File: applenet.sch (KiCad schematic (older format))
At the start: 112 parts, among them J1 6PIN, P1 LISA_BUS, T1 157-0019, T2 157-0020, Y1 Crystal

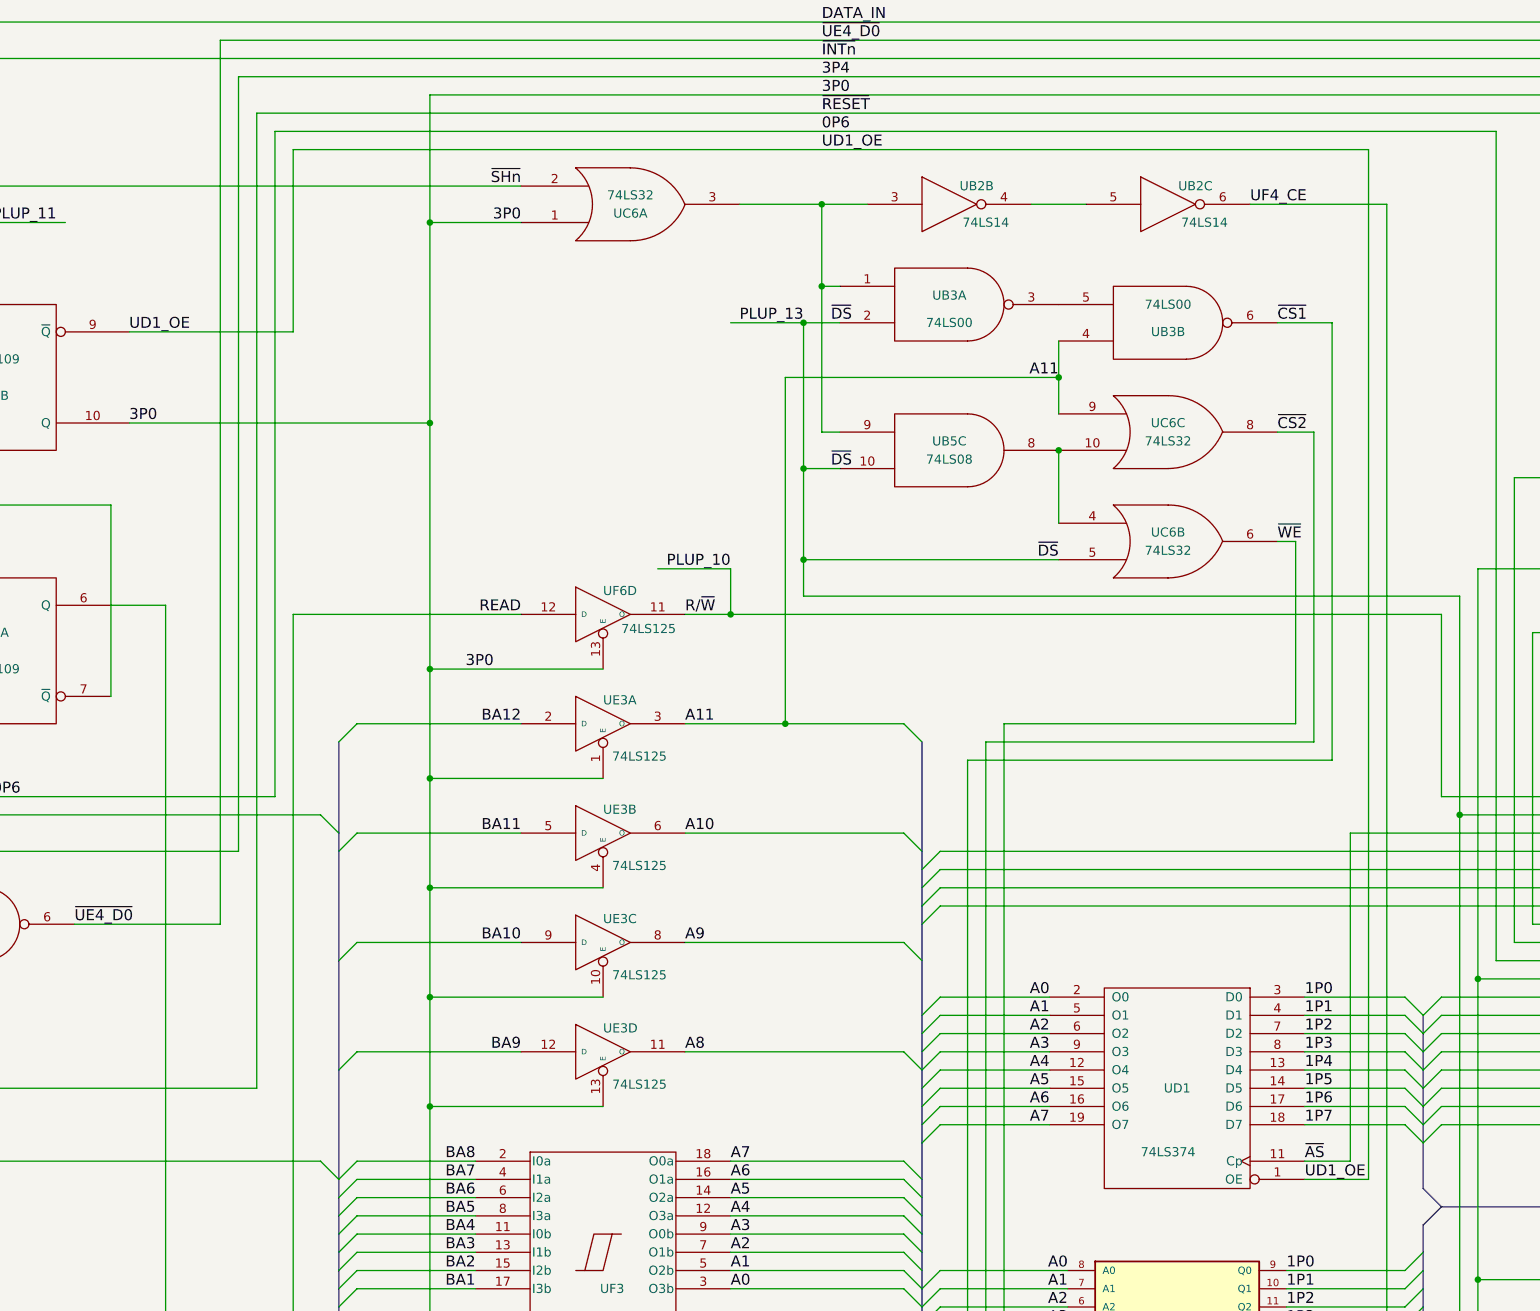
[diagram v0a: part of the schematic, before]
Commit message: Correct input to UC6B.
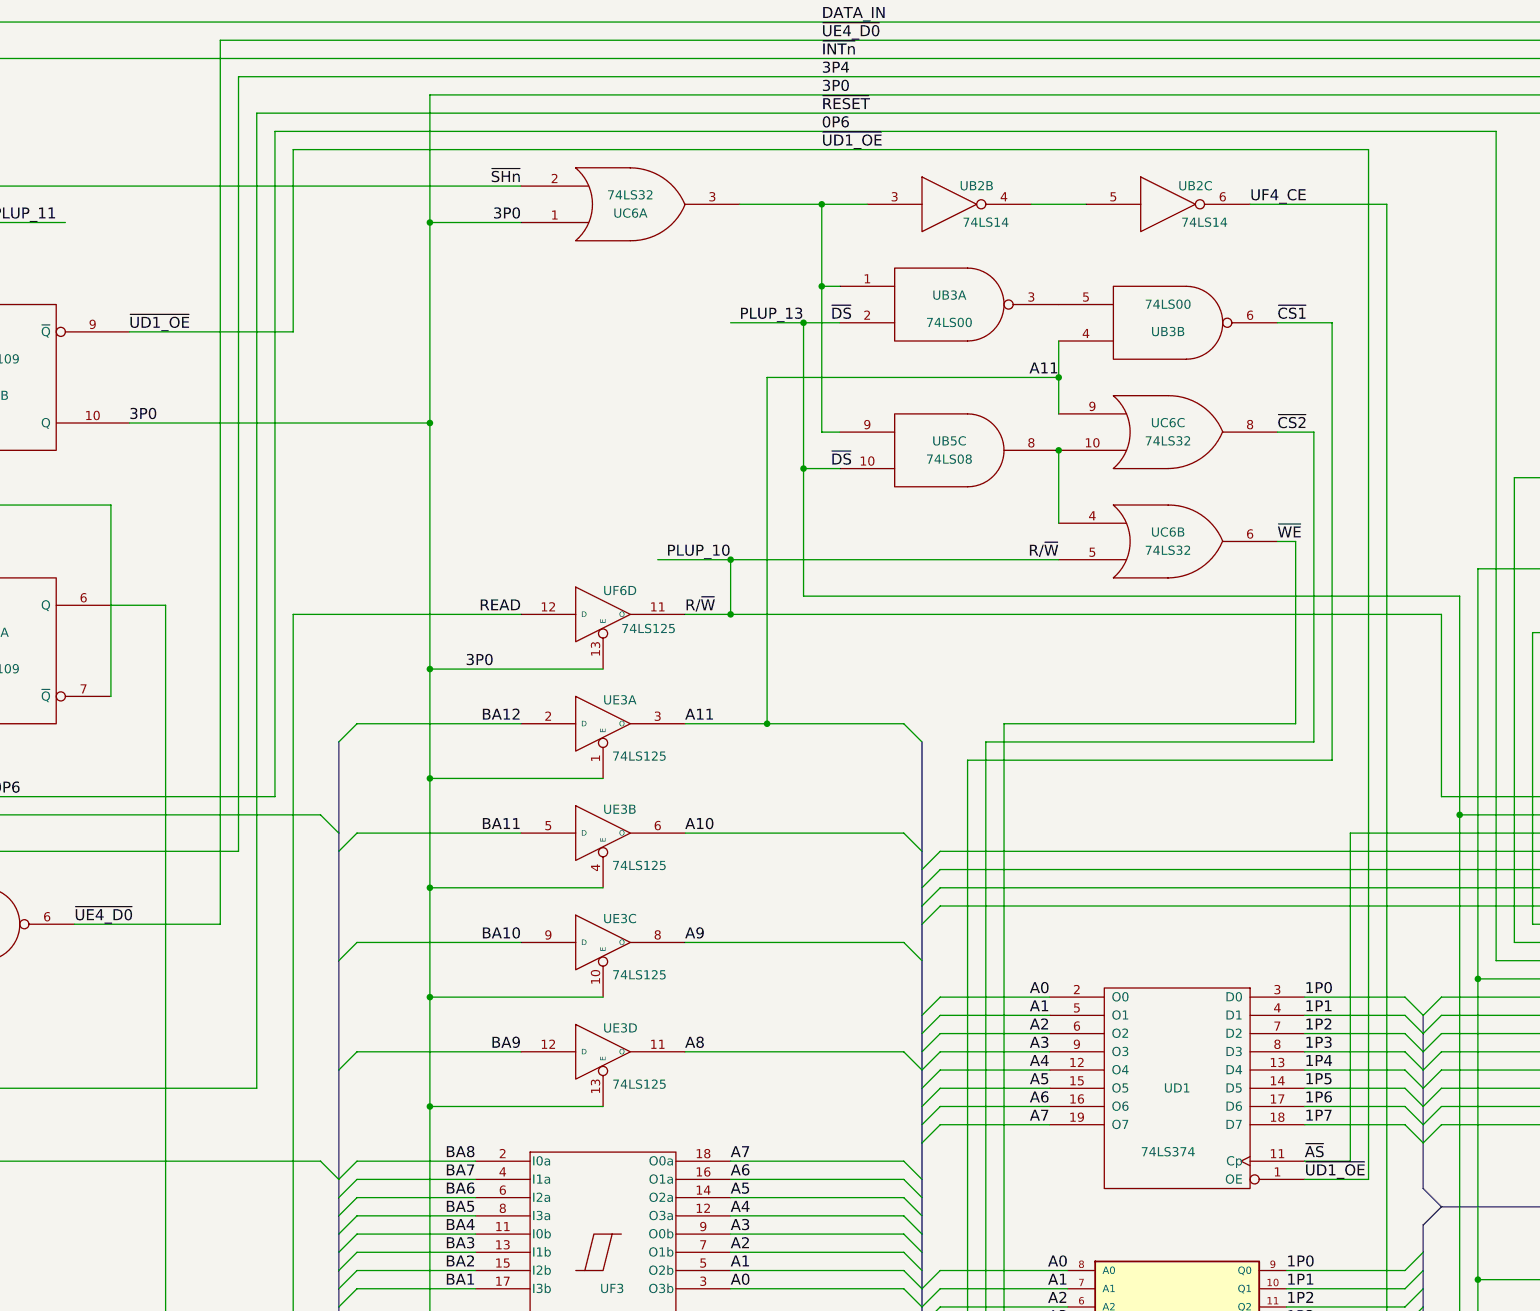
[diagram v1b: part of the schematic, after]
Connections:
- net PLUP_10: now also UC6.5
- net PLUP_13: no longer UC6.5
- net UD1_OE renamed ~UD1_OE
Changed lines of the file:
@@
 Title "Inferred schematic for the AppleNet network adaptor for Lisa"
 Date "2018-11-25"
-Rev "000 (DRAFT!)"
+Rev "001 (DRAFT!)"
 Comp ""
 Comment1 "London"
@@
 ~AS
 Text Label 12500 7550 0    60   ~ 0
-UD1_OE
+~UD1_OE
 Text Label 6050 2900 0    60   ~ 0
-UD1_OE
+~UD1_OE
 Text Label 6050 3400 0    60   ~ 0
 3P0
@@
 ~DS
 Text Label 11150 4150 2    60   ~ 0
-~DS
+R/~W
 Text Label 18450 4900 2    60   ~ 0
 DATA_OUT
@@
 Text Label 18450 5300 0    60   ~ 0
 PLUP_15
-Text Label 9350 4200 2    60   ~ 0
+Text Label 9350 4150 2    60   ~ 0
 PLUP_10
 Text Label 15100 2600 2    60   ~ 0
@@
 ~RESET
 Text Label 9850 1900 0    60   ~ 0
-UD1_OE
+~UD1_OE
 Text Label 9850 1800 0    60   ~ 0
 0P6
@@
 Wire Wire Line
 	9750 4350 13350 4350
+Connection ~ 9550 5050
 Wire Wire Line
-	9750 4150 11150 4150
-Connection ~ 9650 5050
-Wire Wire Line
-	9650 3150 9650 5050
+	9550 3150 9550 5050
 Wire Wire Line
 	12750 7450 12750 5650
@@
 Connection ~ 16800 16600
 Wire Wire Line
-	9100 5050 9650 5050
+	9100 5050 9550 5050
 Wire Wire Line
-	9650 5050 10300 5050
+	9550 5050 10300 5050
 Wire Wire Line
 	7300 6850 8200 6850
@@
 	2250 7450 4100 7450
 Wire Wire Line
-	9650 3150 11150 3150
+	9550 3150 11150 3150
 Wire Wire Line
 	10500 6050 14150 6050
@@
 	9750 2850 9750 3650
 Wire Wire Line
-	9750 3650 9750 4150
+	9750 3650 9750 4350
 Wire Wire Line
-	9750 4150 9750 4350
-Wire Wire Line
-	9950 3650 9750 3650
+	9750 3650 9950 3650
 Wire Wire Line
 	9850 3450 9950 3450
@@
 	8200 2300 7700 2300
 Connection ~ 9750 2850
-Connection ~ 9750 4150
 Connection ~ 18400 5300
 Wire Wire Line
-	9350 4450 9350 4200
+	9350 4450 9350 4150
 Connection ~ 9350 4450
 Wire Wire Line
-	9350 4200 8950 4200
+	8950 4150 9350 4150
+Wire Wire Line
+	9350 4150 11150 4150
 Wire Wire Line
 	1900 4000 2250 4000
@@
 Text Notes 8400 17600 0    138  ~ 0
 CHUNNEL
+Connection ~ 9350 4150
 $EndSCHEMATC

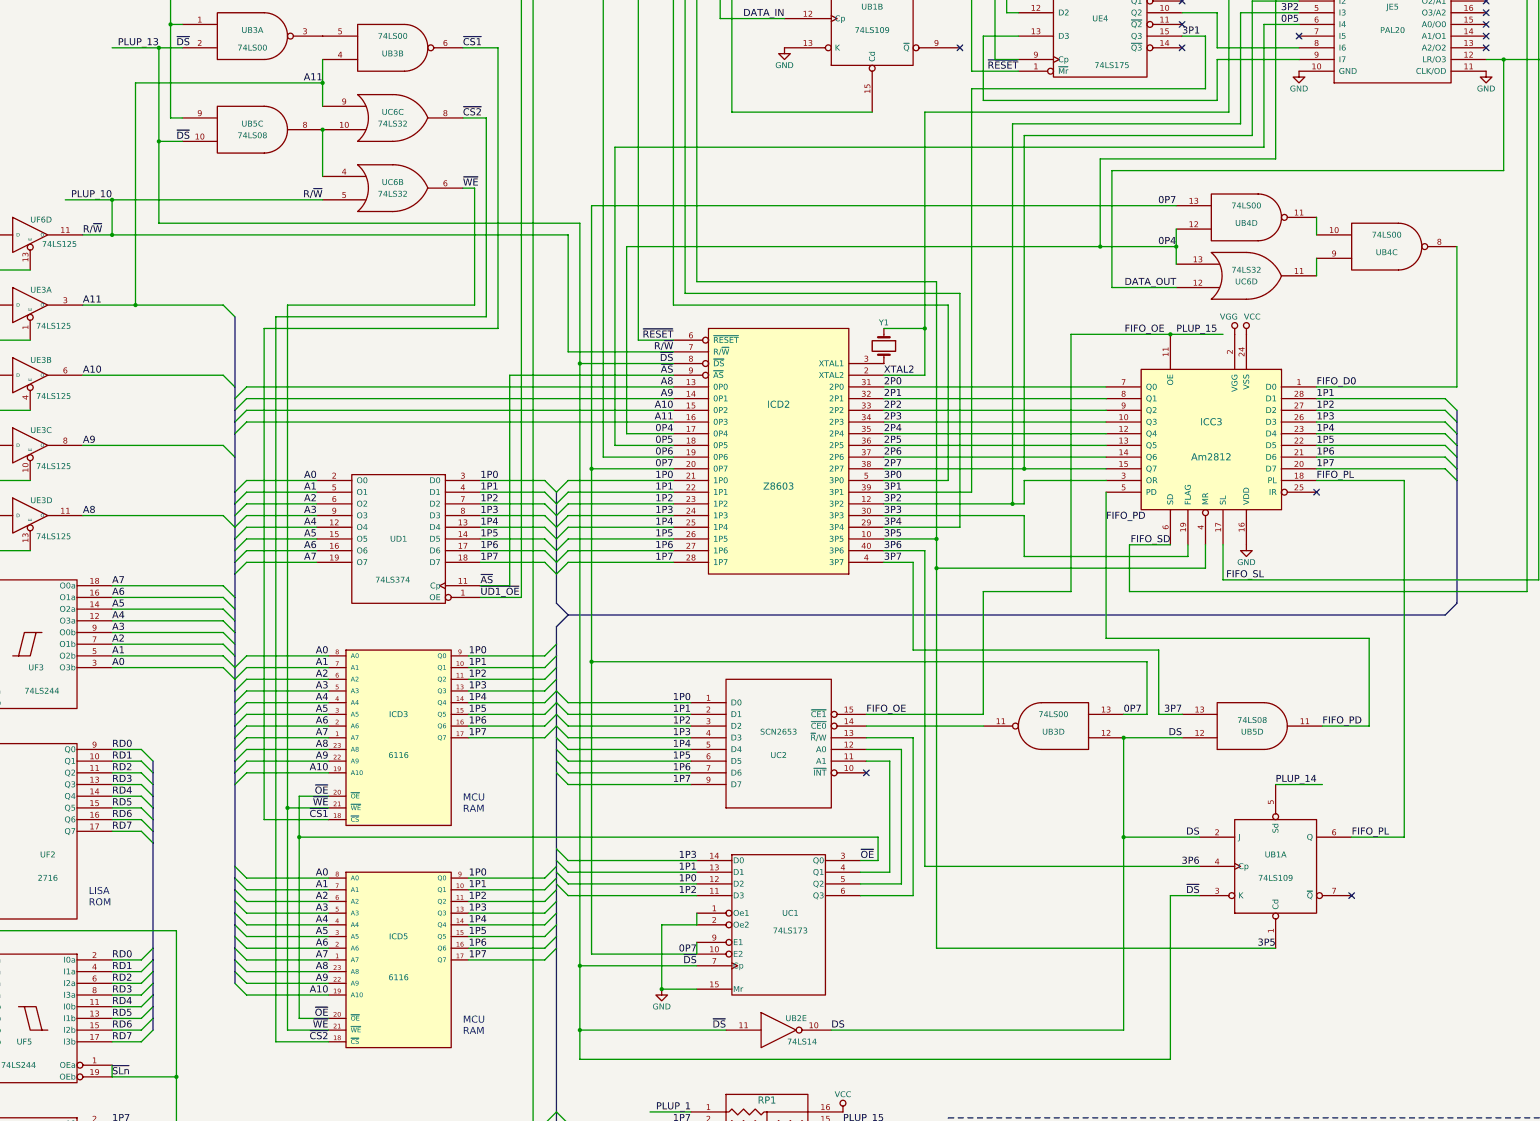
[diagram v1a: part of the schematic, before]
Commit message: Apple part number labeling on custom chips.
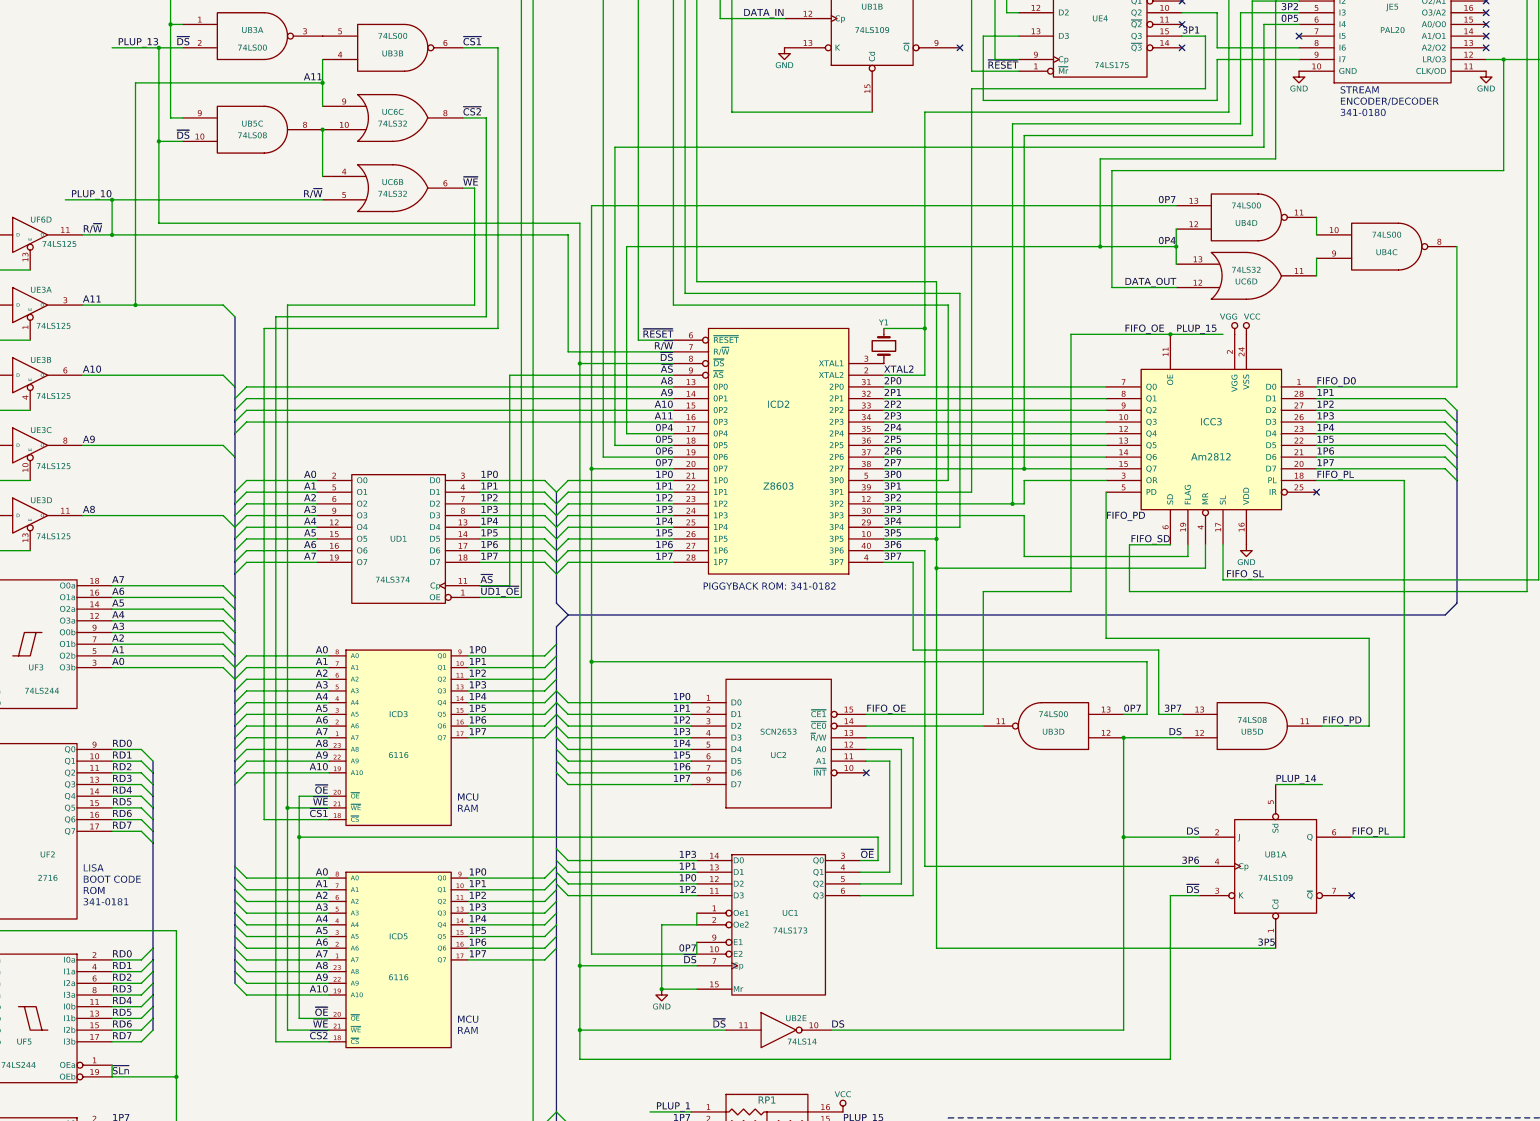
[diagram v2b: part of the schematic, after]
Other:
- note added: "LISA\nBOOT CODE\nROM\n341-0181"
- note added: "PIGGYBACK ROM: 341-0182"
- note added: "STREAM\nENCODER/DECODER\n341-0180"
- note removed: "LISA\nROM"
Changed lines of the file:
@@
 Sheet 1 1
 Title "Inferred schematic for the AppleNet network adaptor for Lisa"
-Date "2018-11-25"
-Rev "001 (DRAFT!)"
+Date "2018-12-03"
+Rev "002 (DRAFT!)"
 Comp ""
 Comment1 "London"
@@
 Text Label 9850 1800 0    60   ~ 0
 0P6
-Text Notes 12350 9400 0    60   ~ 0
+Text Notes 12300 9400 0    60   ~ 0
 MCU\nRAM
-Text Notes 12350 11300 0    60   ~ 0
+Text Notes 12300 11300 0    60   ~ 0
 MCU\nRAM
-Text Notes 9150 10200 0    60   ~ 0
-LISA\nROM
+Text Notes 9100 10200 0    60   ~ 0
+LISA\nBOOT CODE\nROM\n341-0181
 Wire Wire Line
 	2750 13200 9800 13200
@@
 CHUNNEL
 Connection ~ 9350 4150
+Text Notes 19850 3450 0    60   ~ 0
+STREAM\nENCODER/DECODER\n341-0180
+Text Notes 14400 7500 0    60   ~ 0
+PIGGYBACK ROM: 341-0182
 $EndSCHEMATC

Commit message: Revise the network connector; update for KiCad 5; other minor changes
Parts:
- C1, C16, C3: symbol CP1 -> applenet-rescue:CP1
- C10, C11, C13, C14, C15, C18, C19, C2, C20, C21, C22, C23, C24, C25, C26, C27, C28, C29, C30, C31, C32, C33, C34, C35, C36, C37, C38, C39, C4, C40, C41, C5, C6, C7, C8, C9: symbol C -> applenet-rescue:C
- ICC3: symbol Am2812 -> applenet-rescue:Am2812
- ICD2: symbol Z8603 -> applenet-rescue:Z8603
- ICD3, ICD5: symbol 6116 -> applenet-rescue:6116
- J1: symbol 6PIN -> applenet-rescue:6PIN
- JE5: symbol PAL20 -> applenet-rescue:PAL20
- L1, L2, L3, L4, L5, L6: symbol INDUCTOR -> applenet-rescue:INDUCTOR
- P1: symbol LISA_BUS -> applenet-rescue:LISA_BUS
- QA7: symbol CA3146E -> applenet-rescue:CA3146E
- R1, R10, R11, R12, R13, R16, R17, R18, R2, R3, R4, R5, R6, R7, R8, R9: symbol R -> applenet-rescue:R
- R15: symbol Jumper_NO_Small -> applenet-rescue:Jumper_NO_Small
- RP1: symbol 898-1-R3.3K -> applenet-rescue:898-1-R3.3K
- T1: symbol 157-0019 -> applenet-rescue:157-0019
- T2: symbol 157-0020 -> applenet-rescue:157-0020
- TP1, TP10, TP11, TP12, TP13, TP14, TP15, TP16, TP17, TP2, TP3, TP4, TP6, TP7, TP8, TP9: symbol TEST_1P -> applenet-rescue:TEST_1P
- UA1: symbol 74LS123 -> applenet-rescue:74LS123
- UA3: symbol 75107A -> applenet-rescue:75107A
- UB1, UF1: symbol 74LS109 -> applenet-rescue:74LS109
- UB2: symbol 74LS14 -> applenet-rescue:74LS14
- UB3, UB4: symbol 74LS00 -> applenet-rescue:74LS00
- UB5: symbol 74LS08 -> applenet-rescue:74LS08
- UC1: symbol 74LS173 -> applenet-rescue:74LS173
- UC2: symbol SCN2653 -> applenet-rescue:SCN2653
- UC6: symbol 74LS32 -> applenet-rescue:74LS32
- UD1: symbol 74LS374 -> applenet-rescue:74LS374
- UD7: symbol UA733C -> applenet-rescue:UA733C
- UE3, UF6: symbol 74LS125 -> applenet-rescue:74LS125
- UE4: symbol 74LS175 -> applenet-rescue:74LS175
- UE6: symbol 74265 -> applenet-rescue:74265
- UF2: symbol 2716 -> applenet-rescue:2716
- UF3, UF5: symbol 74LS244 -> applenet-rescue:74LS244
- UF4: symbol 74LS245 -> applenet-rescue:74LS245
- UF7: symbol 75453 -> applenet-rescue:75453
- Y1: symbol Crystal -> applenet-rescue:Crystal
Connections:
- net GND: now also J1.1, J1.4; no longer J1.2
- net at T2.4 (P6): now also J1.2; no longer J1.1
- net at J1.5: now also T1.1 (P1); no longer T1.2 (P2)
- net at J1.6: now also T1.2 (P2); no longer T1.3 (P3)
- new net: R1.1, T1.3 (P3)
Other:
- moved on the sheet: C13, C14, C15, C16, J1, L5, R1, R16, R17, R18, T2, TP1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
